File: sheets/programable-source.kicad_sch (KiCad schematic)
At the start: 24 parts, among them Q1 PDTC114EU,115, Q2 DMP2160UW-7, Q3 DMN2058U-7, Q4 DMN2058U-7, U4 MCP6H02T-E/SN

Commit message: Use kicad footprints
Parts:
- D6: footprint Passive:SOD-123_L2.6-W1.7-LS3.5-RD -> Diode_SMD:D_SOD-123
- Q1, Q2: footprint Transistors:SOT-323-3_L2.0-W1.3-P1.30-LS2.1-BR -> Package_TO_SOT_SMD:SOT-323_SC-70
- Q3, Q4: footprint Transistors:SOT-23-3_L2.9-W1.3-P1.90-LS2.4-BR -> Package_TO_SOT_SMD:SOT-23
- U4: footprint ICs:SOIC-8_L4.9-W3.9-P1.27-LS6.0-BL -> Package_SO:SOIC-8_3.9x4.9mm_P1.27mm
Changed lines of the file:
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@@
 			)
 		)
-		(property "Footprint" "Transistors:SOT-323-3_L2.0-W1.3-P1.30-LS2.1-BR"
+		(property "Footprint" "Package_TO_SOT_SMD:SOT-323_SC-70"
 			(at 165.1 73.66 0)
 			(effects
@@
 			)
 		)
-		(property "Footprint" "Transistors:SOT-323-3_L2.0-W1.3-P1.30-LS2.1-BR"
+		(property "Footprint" "Package_TO_SOT_SMD:SOT-323_SC-70"
 			(at 185.42 116.84 0)
 			(effects
@@
 			)
 		)
-		(property "Footprint" "Passive:SOD-123_L2.6-W1.7-LS3.5-RD"
+		(property "Footprint" "Diode_SMD:D_SOD-123"
 			(at 203.2 63.5 0)
 			(effects
@@
 			)
 		)
-		(property "Footprint" "Transistors:SOT-23-3_L2.9-W1.3-P1.90-LS2.4-BR"
+		(property "Footprint" "Package_TO_SOT_SMD:SOT-23"
 			(at 229.87 96.52 0)
 			(effects
@@
 			)
 		)
-		(property "Footprint" "ICs:SOIC-8_L4.9-W3.9-P1.27-LS6.0-BL"
+		(property "Footprint" "Package_SO:SOIC-8_3.9x4.9mm_P1.27mm"
 			(at 110.49 106.68 0)
 			(effects
@@
 			)
 		)
-		(property "Footprint" "ICs:SOIC-8_L4.9-W3.9-P1.27-LS6.0-BL"
+		(property "Footprint" "Package_SO:SOIC-8_3.9x4.9mm_P1.27mm"
 			(at 58.42 109.22 0)
 			(effects
@@
 			)
 		)
-		(property "Footprint" "Transistors:SOT-23-3_L2.9-W1.3-P1.90-LS2.4-BR"
+		(property "Footprint" "Package_TO_SOT_SMD:SOT-23"
 			(at 250.19 105.41 0)
 			(effects

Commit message: add MCU + output
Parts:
- renumbered Q2 to Q1, Q1 to Q2, R14 to R12, R12 to R14, R25 to R19, R19 to R20, R20 to R21, R21 to R22, R22 to R23, R23 to R24, R24 to R25
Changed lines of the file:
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@@
 		(dnp no)
 		(fields_autoplaced yes)
-		(property "Reference" "R22"
+		(property "Reference" "R23"
 			(at 231.14 54.6099 0)
 			(effects
@@
 			(project "esp32-didatic-kit"
 				(path "/f57920a5-fee7-4fe5-a133-e8b36941a5a6/68eb6d36-2b61-4a79-8b9e-43cc2ec0c3c5/3614359f-e98f-4e1e-9c03-7ad0b6a0ef5e"
-					(reference "R22")
+					(reference "R23")
 					(unit 1)
 				)
@@
 		(dnp no)
 		(fields_autoplaced yes)
-		(property "Reference" "Q2"
+		(property "Reference" "Q1"
 			(at 177.8 62.23 90)
 			(effects
@@
 			(project ""
 				(path "/f57920a5-fee7-4fe5-a133-e8b36941a5a6/68eb6d36-2b61-4a79-8b9e-43cc2ec0c3c5/3614359f-e98f-4e1e-9c03-7ad0b6a0ef5e"
-					(reference "Q2")
+					(reference "Q1")
 					(unit 1)
 				)
@@
 		(dnp no)
 		(fields_autoplaced yes)
-		(property "Reference" "R23"
+		(property "Reference" "R24"
 			(at 243.84 54.6099 0)
 			(effects
@@
 			(project "esp32-didatic-kit"
 				(path "/f57920a5-fee7-4fe5-a133-e8b36941a5a6/68eb6d36-2b61-4a79-8b9e-43cc2ec0c3c5/3614359f-e98f-4e1e-9c03-7ad0b6a0ef5e"
-					(reference "R23")
+					(reference "R24")
 					(unit 1)
 				)
@@
 		(dnp no)
 		(fields_autoplaced yes)
-		(property "Reference" "R21"
+		(property "Reference" "R22"
 			(at 217.17 64.77 90)
 			(effects
@@
 			(project "esp32-didatic-kit"
 				(path "/f57920a5-fee7-4fe5-a133-e8b36941a5a6/68eb6d36-2b61-4a79-8b9e-43cc2ec0c3c5/3614359f-e98f-4e1e-9c03-7ad0b6a0ef5e"
-					(reference "R21")
+					(reference "R22")
 					(unit 1)
 				)
@@
 		(on_board yes)
 		(dnp no)
-		(property "Reference" "#PWR06"
+		(property "Reference" "#PWR014"
 			(at 58.42 125.73 0)
 			(effects
@@
 			(project ""
 				(path "/f57920a5-fee7-4fe5-a133-e8b36941a5a6/68eb6d36-2b61-4a79-8b9e-43cc2ec0c3c5/3614359f-e98f-4e1e-9c03-7ad0b6a0ef5e"
-					(reference "#PWR06")
+					(reference "#PWR014")
 					(unit 1)
 				)
@@
 		(dnp no)
 		(fields_autoplaced yes)
-		(property "Reference" "R19"
+		(property "Reference" "R20"
 			(at 190.5 64.77 90)
 			(effects
@@
 			(project "esp32-didatic-kit"
 				(path "/f57920a5-fee7-4fe5-a133-e8b36941a5a6/68eb6d36-2b61-4a79-8b9e-43cc2ec0c3c5/3614359f-e98f-4e1e-9c03-7ad0b6a0ef5e"
-					(reference "R19")
+					(reference "R20")
 					(unit 1)
 				)
@@
 		(dnp no)
 		(fields_autoplaced yes)
-		(property "Reference" "R24"
+		(property "Reference" "R25"
 			(at 260.35 54.6099 0)
 			(effects
@@
 			(project "esp32-didatic-kit"
 				(path "/f57920a5-fee7-4fe5-a133-e8b36941a5a6/68eb6d36-2b61-4a79-8b9e-43cc2ec0c3c5/3614359f-e98f-4e1e-9c03-7ad0b6a0ef5e"
-					(reference "R24")
+					(reference "R25")
 					(unit 1)
 				)
@@
 		(dnp no)
 		(fields_autoplaced yes)
-		(property "Reference" "#PWR08"
+		(property "Reference" "#PWR016"
 			(at 228.6 46.99 0)
 			(effects
@@
 			(project ""
 				(path "/f57920a5-fee7-4fe5-a133-e8b36941a5a6/68eb6d36-2b61-4a79-8b9e-43cc2ec0c3c5/3614359f-e98f-4e1e-9c03-7ad0b6a0ef5e"
-					(reference "#PWR08")
+					(reference "#PWR016")
 					(unit 1)
 				)
@@
 		(dnp no)
 		(fields_autoplaced yes)
-		(property "Reference" "Q1"
+		(property "Reference" "Q2"
 			(at 176.53 99.0599 0)
 			(effects
@@
 			(project ""
 				(path "/f57920a5-fee7-4fe5-a133-e8b36941a5a6/68eb6d36-2b61-4a79-8b9e-43cc2ec0c3c5/3614359f-e98f-4e1e-9c03-7ad0b6a0ef5e"
-					(reference "Q1")
+					(reference "Q2")
 					(unit 1)
 				)
@@
 		(dnp no)
 		(fields_autoplaced yes)
-		(property "Reference" "R25"
+		(property "Reference" "R19"
 			(at 180.34 83.8199 0)
 			(effects
@@
 			(project "esp32-didatic-kit"
 				(path "/f57920a5-fee7-4fe5-a133-e8b36941a5a6/68eb6d36-2b61-4a79-8b9e-43cc2ec0c3c5/3614359f-e98f-4e1e-9c03-7ad0b6a0ef5e"
-					(reference "R25")
+					(reference "R19")
 					(unit 1)
 				)
@@
 		(on_board yes)
 		(dnp no)
-		(property "Reference" "#PWR07"
+		(property "Reference" "#PWR012"
 			(at 33.02 83.82 0)
 			(effects
@@
 			(project "esp32-didatic-kit"
 				(path "/f57920a5-fee7-4fe5-a133-e8b36941a5a6/68eb6d36-2b61-4a79-8b9e-43cc2ec0c3c5/3614359f-e98f-4e1e-9c03-7ad0b6a0ef5e"
-					(reference "#PWR07")
+					(reference "#PWR012")
 					(unit 1)
 				)
@@
 		(dnp no)
 		(fields_autoplaced yes)
-		(property "Reference" "R12"
+		(property "Reference" "R14"
 			(at 58.42 66.04 90)
 			(effects
@@
 			(project ""
 				(path "/f57920a5-fee7-4fe5-a133-e8b36941a5a6/68eb6d36-2b61-4a79-8b9e-43cc2ec0c3c5/3614359f-e98f-4e1e-9c03-7ad0b6a0ef5e"
-					(reference "R12")
+					(reference "R14")
 					(unit 1)
 				)
@@
 		(dnp no)
 		(fields_autoplaced yes)
-		(property "Reference" "#PWR05"
+		(property "Reference" "#PWR013"
 			(at 58.42 83.82 0)
 			(effects
@@
 			(project ""
 				(path "/f57920a5-fee7-4fe5-a133-e8b36941a5a6/68eb6d36-2b61-4a79-8b9e-43cc2ec0c3c5/3614359f-e98f-4e1e-9c03-7ad0b6a0ef5e"
-					(reference "#PWR05")
+					(reference "#PWR013")
 					(unit 1)
 				)
@@
 		(dnp no)
 		(fields_autoplaced yes)
-		(property "Reference" "R20"
+		(property "Reference" "R21"
 			(at 196.85 104.1399 0)
 			(effects
@@
 			(project "esp32-didatic-kit"
 				(path "/f57920a5-fee7-4fe5-a133-e8b36941a5a6/68eb6d36-2b61-4a79-8b9e-43cc2ec0c3c5/3614359f-e98f-4e1e-9c03-7ad0b6a0ef5e"
-					(reference "R20")
+					(reference "R21")
 					(unit 1)
 				)
@@
 		(dnp no)
 		(fields_autoplaced yes)
-		(property "Reference" "#PWR09"
+		(property "Reference" "#PWR015"
 			(at 110.49 83.82 0)
 			(effects
@@
 			(project "esp32-didatic-kit"
 				(path "/f57920a5-fee7-4fe5-a133-e8b36941a5a6/68eb6d36-2b61-4a79-8b9e-43cc2ec0c3c5/3614359f-e98f-4e1e-9c03-7ad0b6a0ef5e"
-					(reference "#PWR09")
+					(reference "#PWR015")
 					(unit 1)
 				)
@@
 		(dnp no)
 		(fields_autoplaced yes)
-		(property "Reference" "R14"
+		(property "Reference" "R12"
 			(at 43.18 105.4099 0)
 			(effects
@@
 			(project "esp32-didatic-kit"
 				(path "/f57920a5-fee7-4fe5-a133-e8b36941a5a6/68eb6d36-2b61-4a79-8b9e-43cc2ec0c3c5/3614359f-e98f-4e1e-9c03-7ad0b6a0ef5e"
-					(reference "R14")
-					(unit 1)
-				)
+					(reference "R12")
+					(unit 1)
+				)

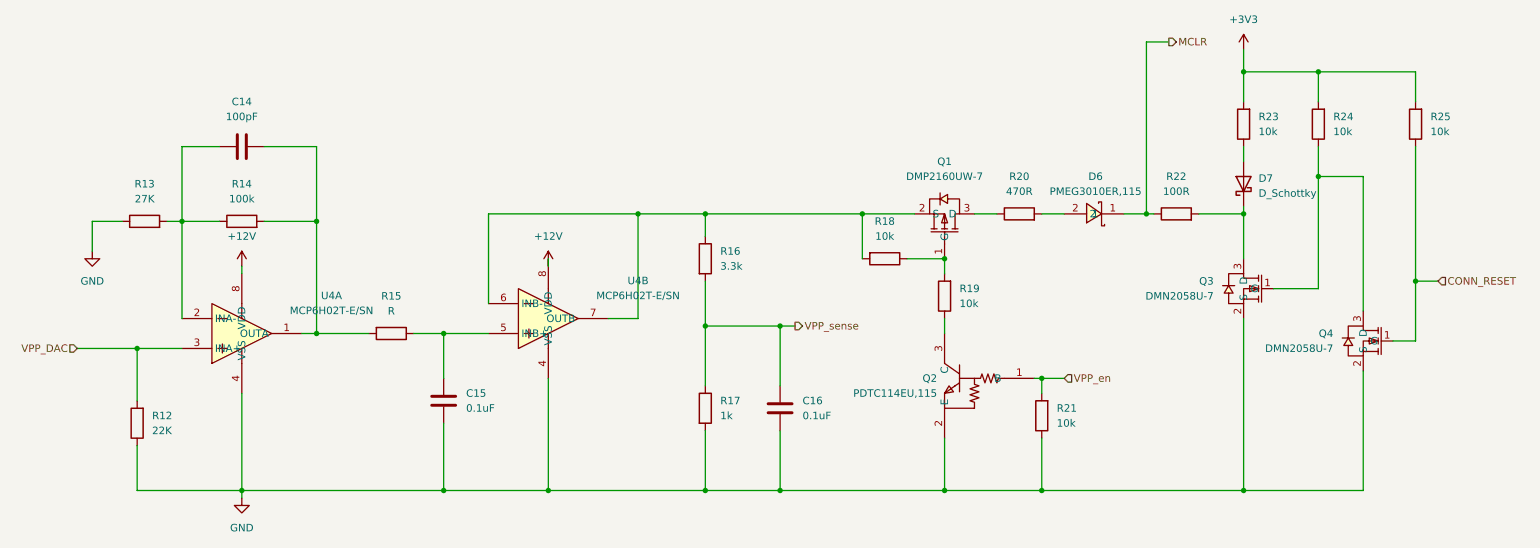
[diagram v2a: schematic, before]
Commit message: Updated MCU to MCU module + set SMD comp. footprints
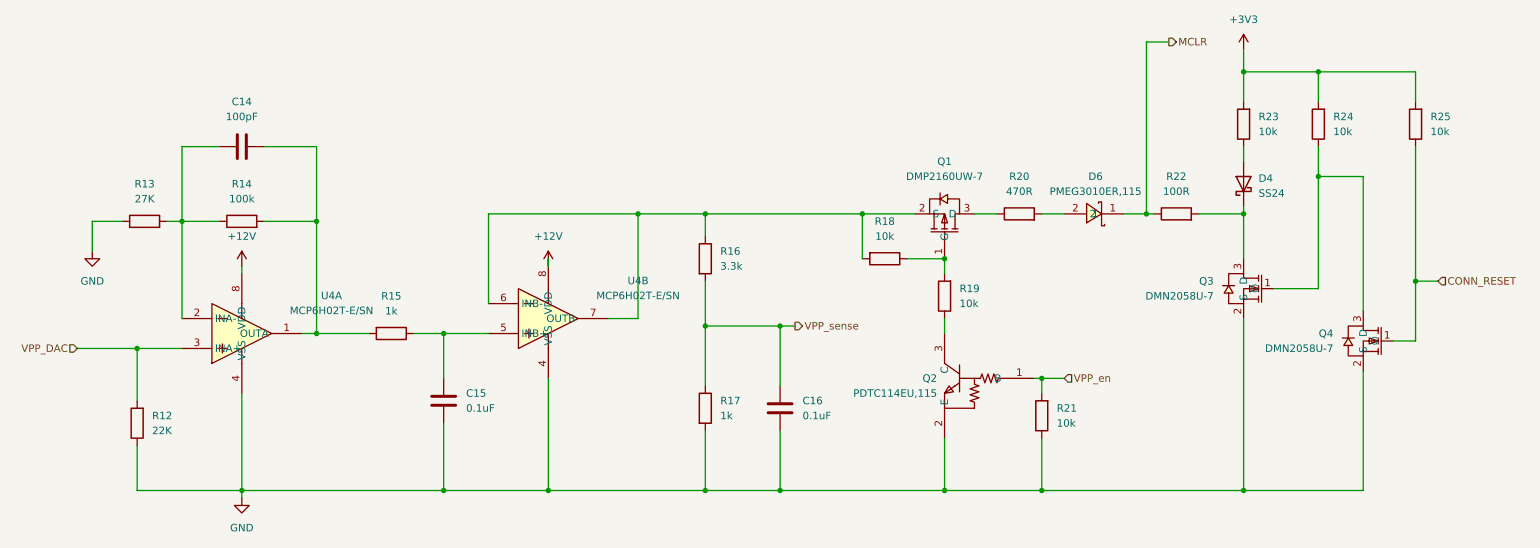
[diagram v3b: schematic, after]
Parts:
- removed D7: D_Schottky, symbol Device:D_Schottky
- added D4: SS24, Diode_SMD:D_SMA, symbol Diode:SS24
- C14, C15, C16: footprint (none) -> Capacitor_SMD:C_0603_1608Metric
- R12, R13, R14, R16, R17, R18, R19, R20, R21, R22, R23, R24, R25: footprint (none) -> Resistor_SMD:R_0603_1608Metric
- R15: value R -> 1k; footprint (none) -> Resistor_SMD:R_0603_1608Metric
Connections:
- net at R23.1: now also D4.2 (A)
- net at Q3.3 (D), R22.2: now also D4.1 (K)
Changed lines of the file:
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@@
 			)
 		)
-		(property "Value" "R"
+		(property "Value" "1k"
 			(at 83.82 87.63 90)
 			(effects
@@
 			)
 		)
-		(property "Footprint" ""
+		(property "Footprint" "Resistor_SMD:R_0603_1608Metric"
 			(at 83.82 89.662 90)
 			(effects
@@
 			)
 		)
-		(property "Footprint" ""
+		(property "Footprint" "Resistor_SMD:R_0603_1608Metric"
 			(at 230.378 55.88 90)
 			(effects
@@
 			)
 		)
-		(property "Footprint" ""
+		(property "Footprint" "Resistor_SMD:R_0603_1608Metric"
 			(at 167.64 76.962 90)
 			(effects
@@
 			)
 		)
-		(property "Footprint" ""
+		(property "Footprint" "Resistor_SMD:R_0603_1608Metric"
 			(at 243.078 55.88 90)
 			(effects
@@
 			)
 		)
-		(property "Footprint" ""
+		(property "Footprint" "Resistor_SMD:R_0603_1608Metric"
 			(at 217.17 72.898 90)
 			(effects
@@
 	)
 	(symbol
-		(lib_id "Device:D_Schottky")
-		(at 228.6 66.04 90)
-		(unit 1)
-		(exclude_from_sim no)
-		(in_bom yes)
-		(on_board yes)
-		(dnp no)
-		(fields_autoplaced yes)
-		(property "Reference" "D7"
-			(at 231.14 65.0874 90)
-			(effects
-				(font
-					(size 1.27 1.27)
-				)
-				(justify right)
-			)
-		)
-		(property "Value" "D_Schottky"
-			(at 231.14 67.6274 90)
-			(effects
-				(font
-					(size 1.27 1.27)
-				)
-				(justify right)
-			)
-		)
-		(property "Footprint" ""
-			(at 228.6 66.04 0)
-			(effects
-				(font
-					(size 1.27 1.27)
-				)
-				(hide yes)
-			)
-		)
-		(property "Datasheet" "~"
-			(at 228.6 66.04 0)
-			(effects
-				(font
-					(size 1.27 1.27)
-				)
-				(hide yes)
-			)
-		)
-		(property "Description" "Schottky diode"
-			(at 228.6 66.04 0)
-			(effects
-				(font
-					(size 1.27 1.27)
-				)
-				(hide yes)
-			)
-		)
-		(pin "1"
-		)
-		(pin "2"
-		)
-		(instances
-			(project ""
-				(path "/f57920a5-fee7-4fe5-a133-e8b36941a5a6/68eb6d36-2b61-4a79-8b9e-43cc2ec0c3c5/3614359f-e98f-4e1e-9c03-7ad0b6a0ef5e"
-					(reference "D7")
-					(unit 1)
-				)
-			)
-		)
-	)
-	(symbol
 		(lib_id "Device:C")
 		(at 58.42 59.69 270)
@@
 			)
 		)
-		(property "Footprint" ""
+		(property "Footprint" "Capacitor_SMD:C_0603_1608Metric"
 			(at 54.61 60.6552 0)
 			(effects
@@
 			)
 		)
-		(property "Footprint" ""
+		(property "Footprint" "Resistor_SMD:R_0603_1608Metric"
 			(at 190.5 72.898 90)
 			(effects
@@
 			)
 		)
-		(property "Footprint" ""
+		(property "Footprint" "Resistor_SMD:R_0603_1608Metric"
 			(at 259.588 55.88 90)
 			(effects
@@
 			)
 		)
-		(property "Footprint" ""
+		(property "Footprint" "Resistor_SMD:R_0603_1608Metric"
 			(at 135.382 78.74 90)
 			(effects
@@
 			)
 		)
-		(property "Footprint" ""
+		(property "Footprint" "Resistor_SMD:R_0603_1608Metric"
 			(at 179.578 85.09 90)
 			(effects
@@
 			)
 		)
-		(property "Footprint" ""
+		(property "Footprint" "Resistor_SMD:R_0603_1608Metric"
 			(at 58.42 74.168 90)
 			(effects
@@
 			)
 		)
-		(property "Footprint" ""
+		(property "Footprint" "Resistor_SMD:R_0603_1608Metric"
 			(at 41.91 74.168 90)
 			(effects
@@
 			)
 		)
-		(property "Footprint" ""
+		(property "Footprint" "Resistor_SMD:R_0603_1608Metric"
 			(at 135.382 104.14 90)
 			(effects
@@
 	)
 	(symbol
+		(lib_id "Diode:SS24")
+		(at 228.6 66.04 90)
+		(unit 1)
+		(exclude_from_sim no)
+		(in_bom yes)
+		(on_board yes)
+		(dnp no)
+		(fields_autoplaced yes)
+		(property "Reference" "D4"
+			(at 231.14 65.0874 90)
+			(effects
+				(font
+					(size 1.27 1.27)
+				)
+				(justify right)
+			)
+		)
+		(property "Value" "SS24"
+			(at 231.14 67.6274 90)
+			(effects
+				(font
+					(size 1.27 1.27)
+				)
+				(justify right)
+			)
+		)
+		(property "Footprint" "Diode_SMD:D_SMA"
+			(at 233.045 66.04 0)
+			(effects
+				(font
+					(size 1.27 1.27)
+				)
+				(hide yes)
+			)
+		)
+		(property "Datasheet" "https://www.vishay.com/docs/88748/ss22.pdf"
+			(at 228.6 66.04 0)
+			(effects
+				(font
+					(size 1.27 1.27)
+				)
+				(hide yes)
+			)
+		)
+		(property "Description" "40V 2A Schottky Diode, SMA"
+			(at 228.6 66.04 0)
+			(effects
+				(font
+					(size 1.27 1.27)
+				)
+				(hide yes)
+			)
+		)
+		(pin "1"
+		)
+		(pin "2"
+		)
+		(instances
+			(project ""
+				(path "/f57920a5-fee7-4fe5-a133-e8b36941a5a6/68eb6d36-2b61-4a79-8b9e-43cc2ec0c3c5/3614359f-e98f-4e1e-9c03-7ad0b6a0ef5e"
+					(reference "D4")
+					(unit 1)
+				)
+			)
+		)
+	)
+	(symbol
 		(lib_id "ICs:MCP6H02T-E_SN")
 		(at 58.42 91.44 0)
@@
 			)
 		)
-		(property "Footprint" ""
+		(property "Footprint" "Capacitor_SMD:C_0603_1608Metric"
 			(at 150.8252 107.95 0)
 			(effects
@@
 			)
 		)
-		(property "Footprint" ""
+		(property "Footprint" "Capacitor_SMD:C_0603_1608Metric"
 			(at 93.6752 106.68 0)
 			(effects
@@
 			)
 		)
-		(property "Footprint" ""
+		(property "Footprint" "Resistor_SMD:R_0603_1608Metric"
 			(at 196.088 105.41 90)
 			(effects
@@
 			)
 		)
-		(property "Footprint" ""
+		(property "Footprint" "Resistor_SMD:R_0603_1608Metric"
 			(at 42.418 106.68 90)
 			(effects
